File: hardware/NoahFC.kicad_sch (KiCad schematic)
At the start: 50 parts, among them J1 ALE, J10 ESC-, J11 CAM, J12 VTX, J2 ELE, J3 VCC, J4 FTDI, J5 GND, J6 THR, J7 PPM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

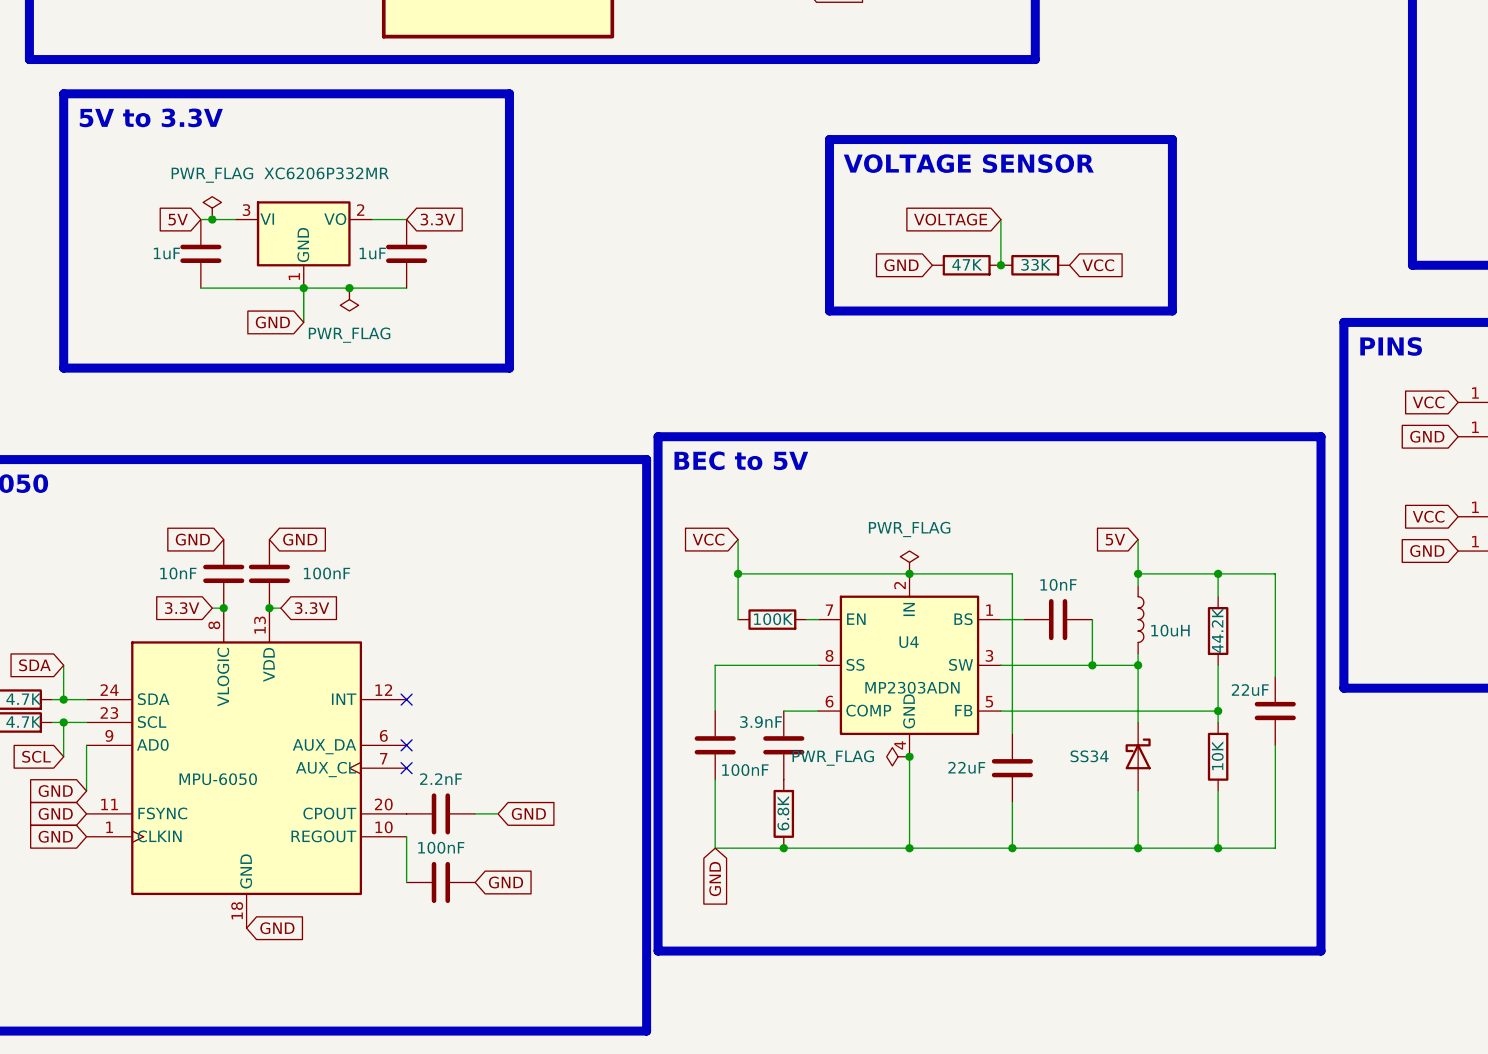
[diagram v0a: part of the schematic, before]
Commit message: replace buck converter with LM317
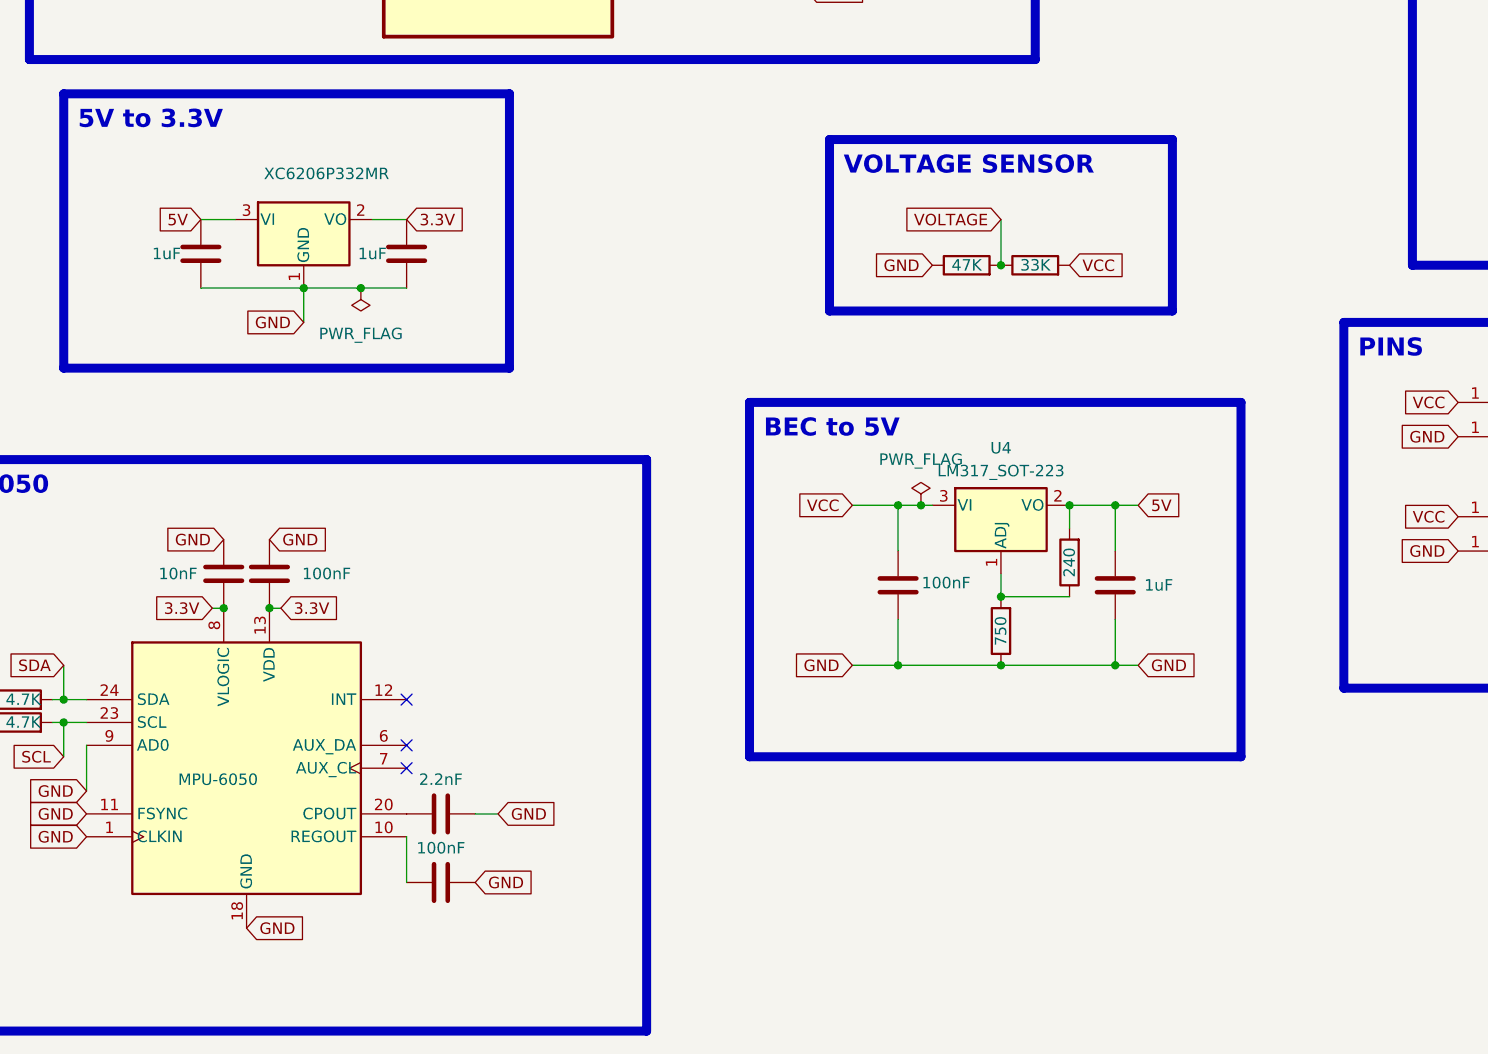
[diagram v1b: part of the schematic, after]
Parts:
- removed C13, C15: 22uF, Capacitor_SMD:C_0805_2012Metric, symbol Device:C
- removed C14: 10nF, Capacitor_SMD:C_0805_2012Metric, symbol Device:C
- removed D4: SS34, Diode_SMD:Nexperia_CFP3_SOD-123W, symbol Diode:1N5822
- removed L1: 10uH, Inductor_SMD:L_7.3x7.3_H3.5, symbol Device:L
- removed R13: 44.2K, Resistor_SMD:R_0805_2012Metric, symbol Device:R
- removed R14: 10K, Resistor_SMD:R_0805_2012Metric, symbol Device:R
- removed R6: 100K, Resistor_SMD:R_0805_2012Metric, symbol Device:R
- removed U4: MP2303ADN, Package_SO:SOIC-8_3.9x4.9mm_P1.27mm, symbol Regulator_Switching:MP2303ADN
- added R2: 240, Resistor_SMD:R_0805_2012Metric, symbol Device:R
- added U4: LM317_SOT-223, Package_TO_SOT_SMD:SOT-223-3_TabPin2, symbol Regulator_Linear:LM317_SOT-223
- C12: value 3.9nF -> 1uF
- R11: value 6.8K -> 750
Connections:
- net 5V: now also C12.2, R2.2, U4.2 (VO)
- net GND: now also C12.1
- net VCC: now also C5.2, U4.3 (VI)
- net at R11.2: now also R2.1, U4.1 (ADJ); no longer C12.1

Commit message: update to rev7 board
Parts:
- removed U5: MAX7456EUI+, SOP65P637X110-28N, symbol MAX7456EUI_:MAX7456EUI+
- added J13: ESC_GND, TestPoint:TestPoint_Pad_1.0x1.0mm, symbol Connector:Conn_01x01_Socket
- added J14: ESC_PWM, TestPoint:TestPoint_Pad_1.0x1.0mm, symbol Connector:Conn_01x01_Socket
- added J15: BEC+, TestPoint:TestPoint_Pad_2.0x2.0mm, symbol Connector:Conn_01x01_Socket
- added J16: BEC-, TestPoint:TestPoint_Pad_2.0x2.0mm, symbol Connector:Conn_01x01_Socket
- added U6: MAX7456EUI+, MAX7456:SOP65P637X110-28N, symbol MAX7456EUI:MAX7456EUI+
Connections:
- net 5V: now also U6.19 (~{RESET}), U6.21 (AVDD), U6.24 (PVDD), U6.3 (DVDD); no longer J1.2 (Pin_2), J2.2 (Pin_2), J6.2 (Pin_2), J7.2 (Pin_2)
- net GND: now also J13.1 (Pin_1), J16.1 (Pin_1), U6.20 (AGND), U6.23 (PGND), U6.4 (DGND)
- net MISO: now also U6.11 (SDOUT)
- net MOSI: now also U6.9 (SDIN)
- net SAG: now also U6.25 (SAG)
- net SCK: now also U6.10 (SCLK)
- net SS: now also U6.8 (~{CS})
- net THROTTLE: now also J14.1 (Pin_1)
- net VIN: now also U6.22 (VIN)
- net VOUT: now also U6.26 (VOUT)
- net XTAL1_OSD: now also U6.5 (CLKIN)
- net XTAL2_OSD: now also U6.6 (XFB)
- new net BEC_5V: J1.2 (Pin_2), J15.1 (Pin_1), J2.2 (Pin_2), J6.2 (Pin_2), J7.2 (Pin_2)
- no-connect marks 17 -> 16

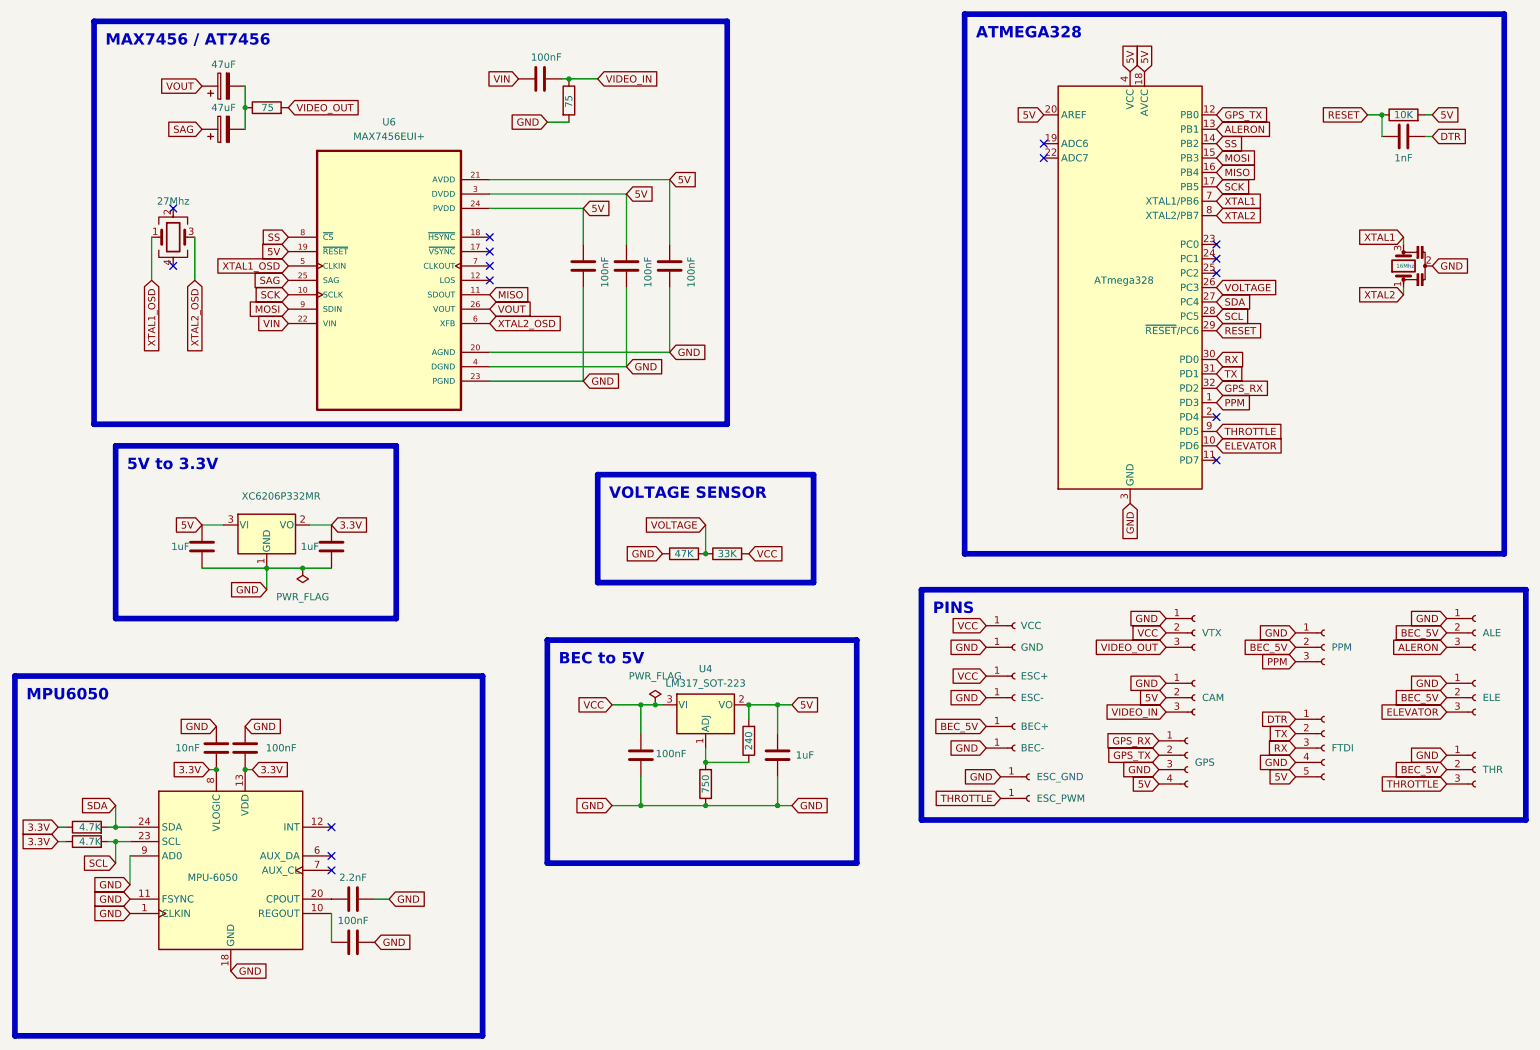
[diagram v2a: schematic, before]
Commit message: update project with LCSC parts, fix some component prepare rev8
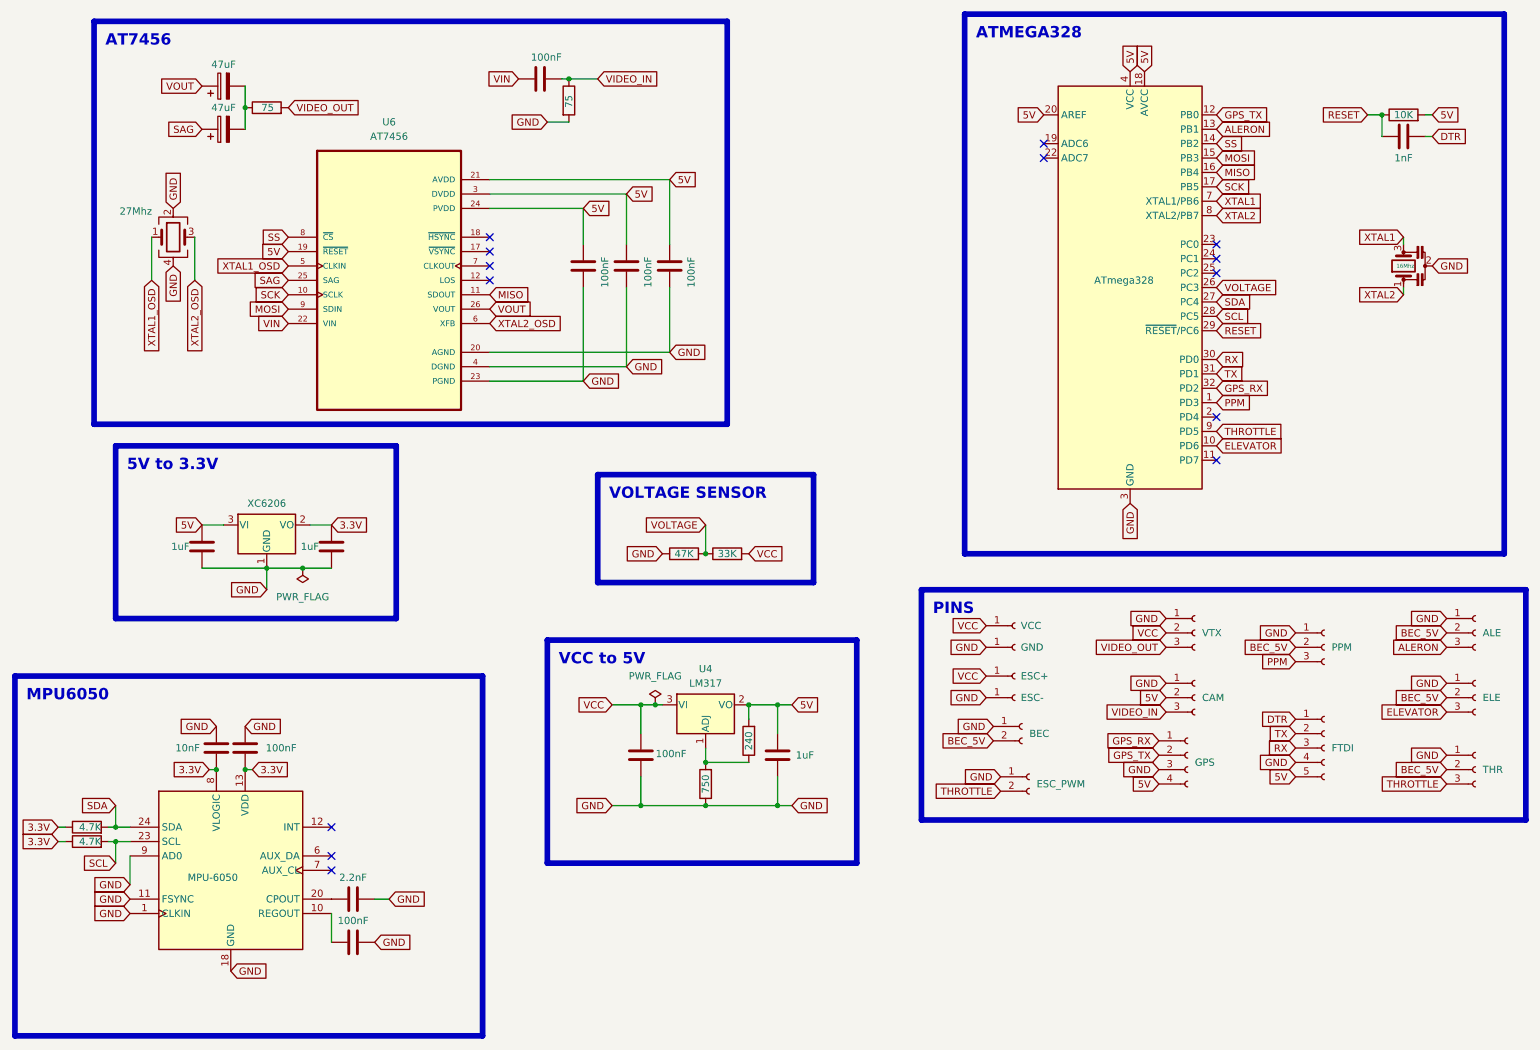
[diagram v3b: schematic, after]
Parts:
- removed J13: ESC_GND, TestPoint:TestPoint_Pad_1.0x1.0mm, symbol Connector:Conn_01x01_Socket
- removed J14: ESC_PWM, TestPoint:TestPoint_Pad_1.0x1.0mm, symbol Connector:Conn_01x01_Socket
- removed J15: BEC+, TestPoint:TestPoint_Pad_2.0x2.0mm, symbol Connector:Conn_01x01_Socket
- removed J16: BEC-, TestPoint:TestPoint_Pad_2.0x2.0mm, symbol Connector:Conn_01x01_Socket
- added J15: ESC_PWM, Connector_PinHeader_2.00mm:PinHeader_1x02_P2.00mm_Vertical, symbol Connector:Conn_01x02_Socket
- added J17: BEC, Connector_PinHeader_2.54mm:PinHeader_1x02_P2.54mm_Vertical, symbol Connector:Conn_01x02_Socket
- C1, C17, C2, C4, C5, C7, C8: LCSC (none) -> C49678
- C10, C11, C12: LCSC (none) -> C28323
- C18, C19: LCSC (none) -> C131173
- C3: LCSC (none) -> C94121
- C6: LCSC (none) -> C1710
- C9: LCSC (none) -> C28260
- J1, J11, J12, J2, J6, J7: LCSC (none) -> C42431836
- J4: LCSC (none) -> C160391
- J8: LCSC (none) -> C160390
- R1: LCSC (none) -> C84376
- R10, R9: LCSC (none) -> C2974040
- R11: LCSC (none) -> C114546
- R2: LCSC (none) -> C17572
- R4: LCSC (none) -> C17713
- R5: LCSC (none) -> C2933415
- R7, R8: LCSC (none) -> C17673
- U1: LCSC (none) -> C618731
- U2: LCSC (none) -> C24112
- U3: value XC6206P332MR -> XC6206; LCSC (none) -> C3015484
- U4: value LM317_SOT-223 -> LM317; LCSC (none) -> C68487
- U6: value MAX7456EUI+ -> AT7456; LCSC (none) -> C82351
- Y1: LCSC (none) -> C882606
- Y3: LCSC (none) -> C5444552
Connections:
- net BEC_5V: now also J17.2 (Pin_2)
- net GND: now also Y3.2, Y3.4, J15.1 (Pin_1), J17.1 (Pin_1)
- net THROTTLE: now also J15.2 (Pin_2)
- no-connect marks 16 -> 14

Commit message: add jumpers for vtx
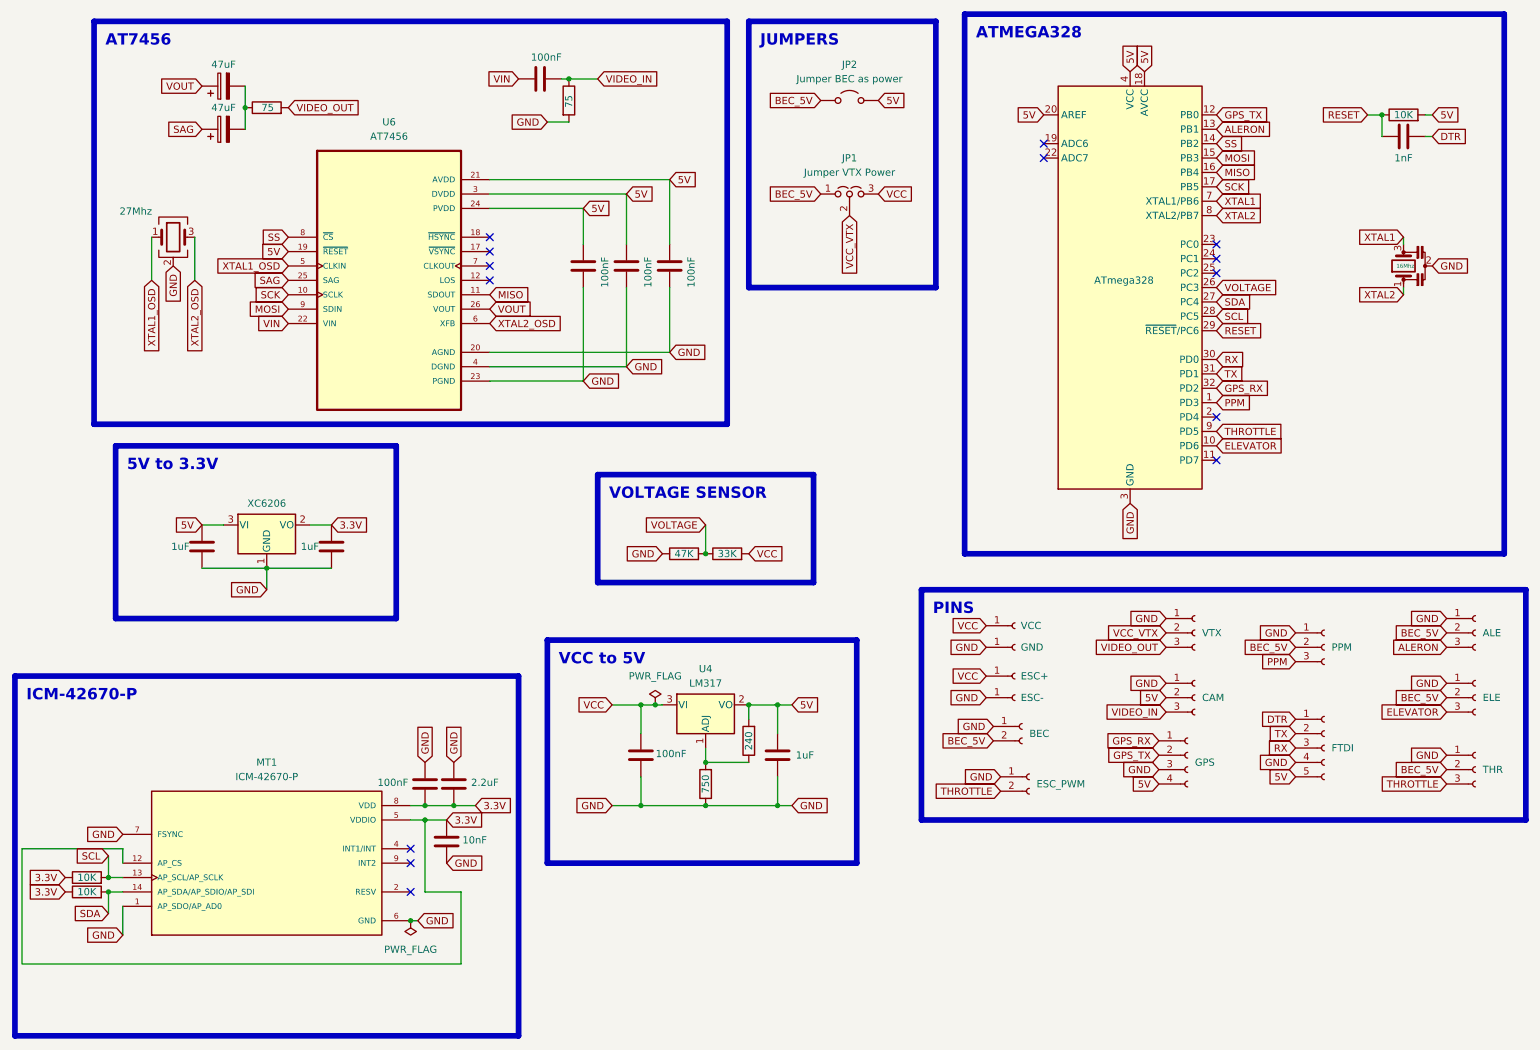
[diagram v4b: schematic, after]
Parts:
- removed C6: 10nF, Capacitor_SMD:C_0805_2012Metric, symbol Device:C
- removed C7, C8: 100nF, Capacitor_SMD:C_0805_2012Metric, symbol Device:C
- removed C9: 2.2nF, Capacitor_SMD:C_0805_2012Metric, symbol Device:C
- removed R7, R8: 4.7K, Resistor_SMD:R_0805_2012Metric, symbol Device:R
- removed U2: MPU-6050, Sensor_Motion:InvenSense_QFN-24_4x4mm_P0.5mm, symbol Sensor_Motion:MPU-6050
- added C13: 100nF, Capacitor_SMD:C_0805_2012Metric_Pad1.18x1.45mm_HandSolder, symbol Device:C
- added C14: 10nF, Capacitor_SMD:C_0805_2012Metric_Pad1.18x1.45mm_HandSolder, symbol Device:C
- added C15: 2.2uF, Capacitor_SMD:C_0805_2012Metric_Pad1.18x1.45mm_HandSolder, symbol Device:C
- added JP1: Jumper VTX Power, Jumper:SolderJumper-3_P1.3mm_Open_RoundedPad1.0x1.5mm, symbol Jumper:Jumper_3_Open
- added JP2: Jumper BEC as power, Jumper:SolderJumper-2_P1.3mm_Open_RoundedPad1.0x1.5mm, symbol Jumper:Jumper_2_Open
- added MT1: ICM-42670-P, ICM:XDCR_ICM-42670-P, symbol ICM-42670-P:ICM-42670-P
- added R3, R6: 10K, Resistor_SMD:R_0805_2012Metric_Pad1.20x1.40mm_HandSolder, symbol Device:R
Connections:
- net 3.3V: now also C13.2, C14.1, C15.2, MT1.12 (AP_CS), MT1.5 (VDDIO), MT1.8 (VDD), R3.1, R6.1
- net 5V: now also JP2.2 (B)
- net BEC_5V: now also JP1.1 (A), JP2.1 (A)
- net GND: now also C13.1, C14.2, C15.1, MT1.1 (AP_SDO/AP_AD0), MT1.6 (GND), MT1.7 (FSYNC)
- net SCL: now also MT1.13 (AP_SCL/AP_SCLK), R3.2
- net SDA: now also MT1.14 (AP_SDA/AP_SDIO/AP_SDI), R6.2
- net VCC: now also JP1.3 (B); no longer J12.2 (Pin_2)
- new net: MT1.10 (RESV), MT1.11 (RESV), MT1.2 (RESV), MT1.3 (RESV)
- new net VCC_VTX: J12.2 (Pin_2), JP1.2 (C)
